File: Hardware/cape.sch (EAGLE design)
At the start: 35 parts, among them IC2 74VHC541, IC4 74VHC541, IC5 74VHC541, J3 RJ45-8P8C, Q1 N-MOSFET-DUALSO8, Q10 N-MOSFET-DUALSO8, Q11 N-MOSFET-DUALSO8, Q12 N-MOSFET-DUALSO8, Q13 N-MOSFET-DUALSO8, Q14 N-MOSFET-DUALSO8, Q15 N-MOSFET-DUALSO8, Q16 N-MOSFET-DUALSO8, Q2 N-MOSFET-DUALSO8, Q3 N-MOSFET-DUALSO8, Q4 N-MOSFET-DUALSO8, Q5 N-MOSFET-DUALSO8, Q6 N-MOSFET-DUALSO8, Q7 N-MOSFET-DUALSO8, Q8 N-MOSFET-DUALSO8, Q9 N-MOSFET-DUALSO8

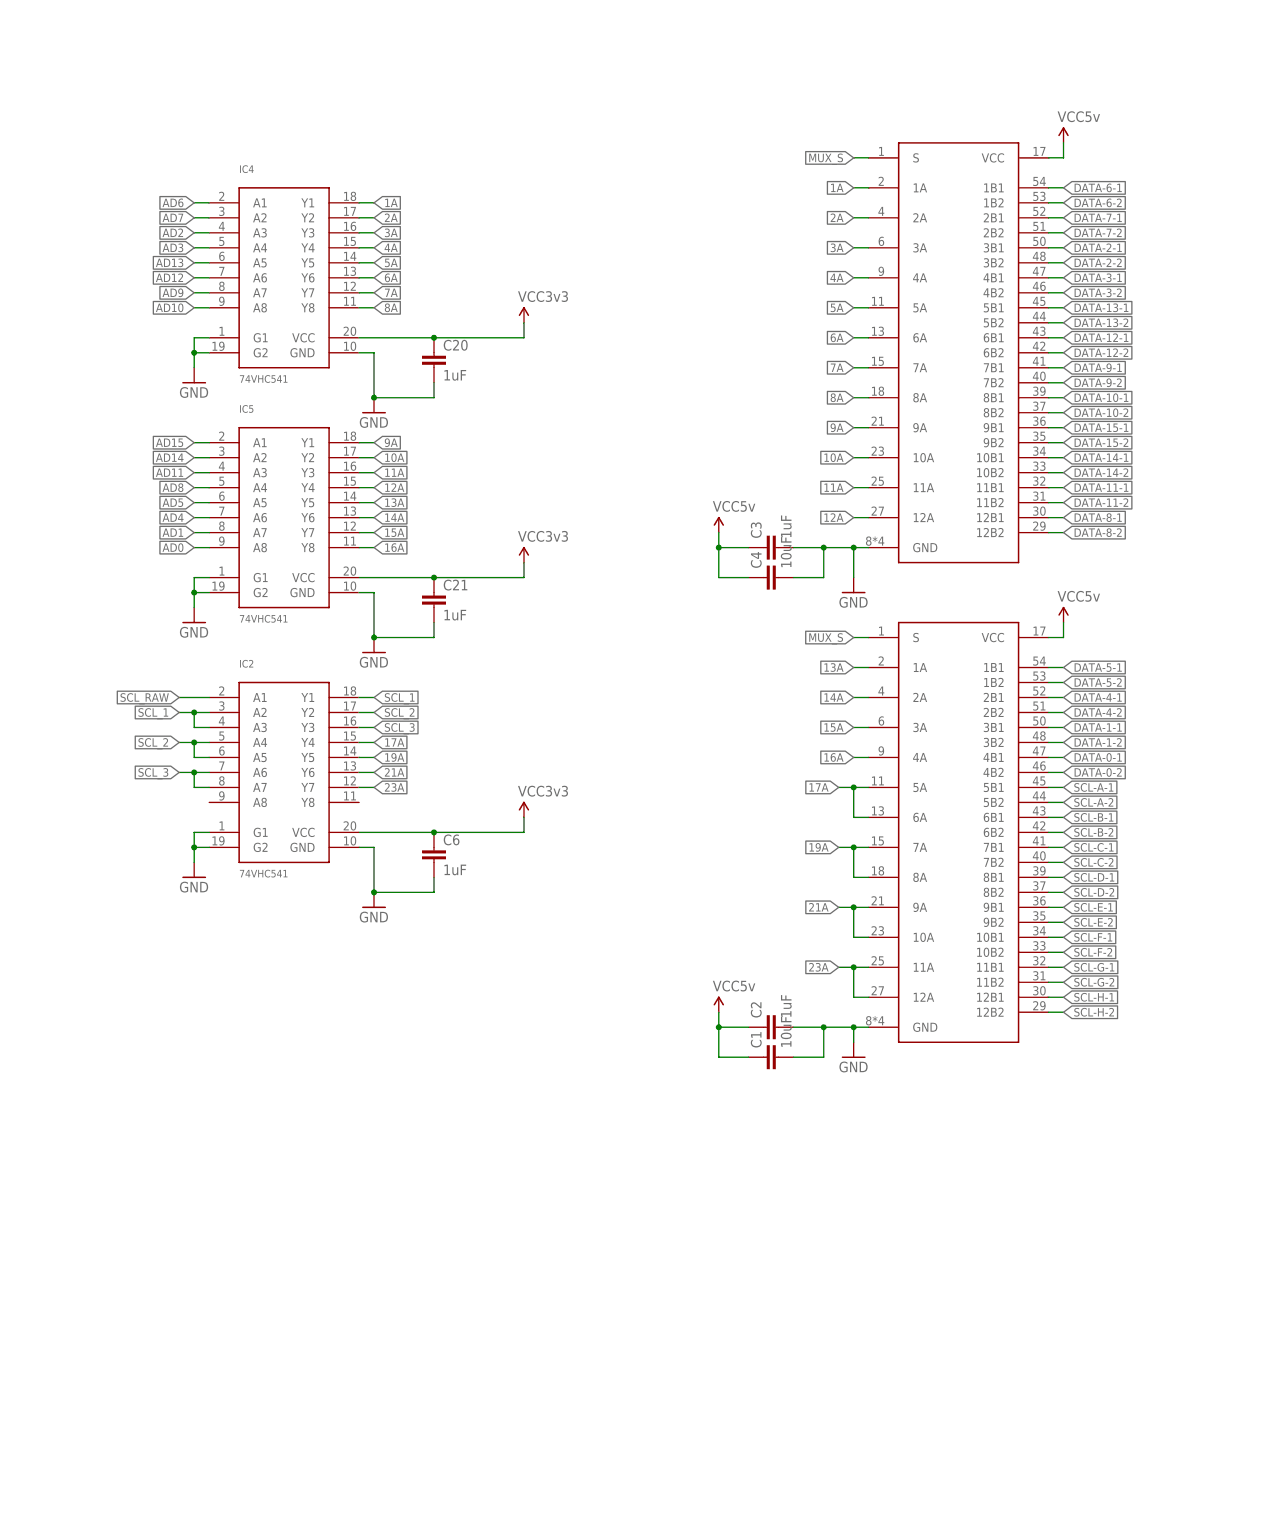
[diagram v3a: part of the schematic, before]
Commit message: Ripped up, starting over with new buffers
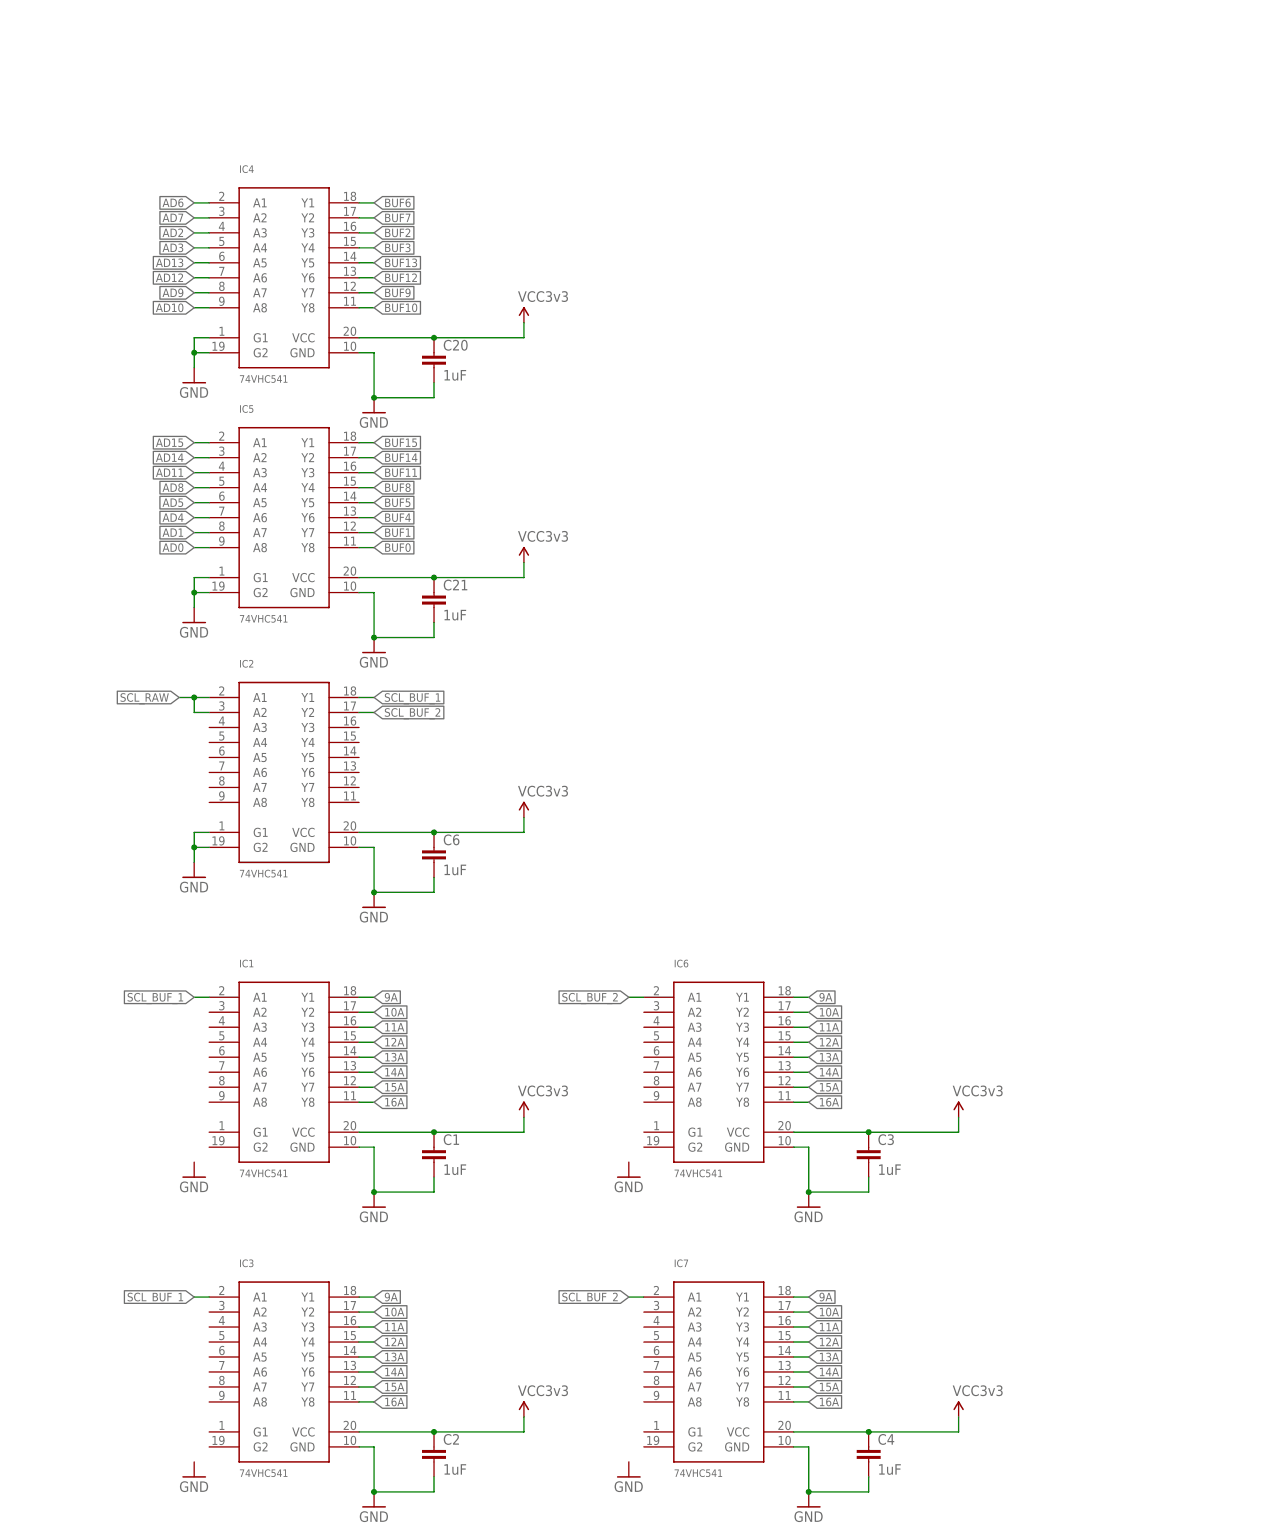
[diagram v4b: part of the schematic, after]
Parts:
- removed U$7, U$8: SN74CBT16292DLRSSOP56, cape:SN74CBT16292DLRSSOP56
- added IC1, IC3, IC6, IC7: 74VHC541, cape:74VHC541
- C1, C4: value 10uF -> 1uF
- IC2, IC4, IC5: PARTNO 74VHC541FT(BE) -> (none)
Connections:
- removed net 17A: IC2.Y4, U$8.5A, U$8.6A
- removed net 19A: IC2.Y5, U$8.7A, U$8.8A
- removed net 1A: IC4.Y1, U$7.1A
- removed net 21A: IC2.Y6, U$8.10A, U$8.9A
- removed net 23A: IC2.Y7, U$8.11A, U$8.12A
- removed net 2A: IC4.Y2, U$7.2A
- removed net 3A: IC4.Y3, U$7.3A
- removed net 4A: IC4.Y4, U$7.4A
- removed net 5A: IC4.Y5, U$7.5A
- removed net 6A: IC4.Y6, U$7.6A
- removed net 7A: IC4.Y7, U$7.7A
- removed net 8A: IC4.Y8, U$7.8A
- removed net SCL_1: IC2.A2, IC2.A3, IC2.Y1
- removed net SCL_2: IC2.A4, IC2.A5, IC2.Y2
- removed net SCL_3: IC2.A6, IC2.A7, IC2.Y3
- new net BUF0: IC5.Y8
- new net BUF1: IC5.Y7
- new net BUF10: IC4.Y8
- new net BUF11: IC5.Y3
- new net BUF12: IC4.Y6
- new net BUF13: IC4.Y5
- new net BUF14: IC5.Y2
- new net BUF15: IC5.Y1
- new net BUF2: IC4.Y3
- new net BUF3: IC4.Y4
- new net BUF4: IC5.Y6
- new net BUF5: IC5.Y5
- new net BUF6: IC4.Y1
- new net BUF7: IC4.Y2
- new net BUF8: IC5.Y4
- new net BUF9: IC4.Y7
- new net SCL_BUF_1: IC1.A1, IC2.Y1, IC3.A1
- new net SCL_BUF_2: IC2.Y2, IC6.A1, IC7.A1
- net 10A: now also IC1.Y2, IC3.Y2, IC6.Y2, IC7.Y2; no longer IC5.Y2, U$7.10A
- net 11A: now also IC1.Y3, IC3.Y3, IC6.Y3, IC7.Y3; no longer IC5.Y3, U$7.11A
- net 12A: now also IC1.Y4, IC3.Y4, IC6.Y4, IC7.Y4; no longer IC5.Y4, U$7.12A
- net 13A: now also IC1.Y5, IC3.Y5, IC6.Y5, IC7.Y5; no longer IC5.Y5, U$8.1A
- net 14A: now also IC1.Y6, IC3.Y6, IC6.Y6, IC7.Y6; no longer IC5.Y6, U$8.2A
- net 15A: now also IC1.Y7, IC3.Y7, IC6.Y7, IC7.Y7; no longer IC5.Y7, U$8.3A
- net 16A: now also IC1.Y8, IC3.Y8, IC6.Y8, IC7.Y8; no longer IC5.Y8, U$8.4A
- net 9A: now also IC1.Y1, IC3.Y1, IC6.Y1, IC7.Y1; no longer IC5.Y1, U$7.9A
- net DATA-0-1: no longer U$8.4B1
- net DATA-0-2: no longer U$8.4B2
- net DATA-1-1: no longer U$8.3B1
- net DATA-1-2: no longer U$8.3B2
- net DATA-10-1: no longer U$7.8B1
- net DATA-10-2: no longer U$7.8B2
- net DATA-11-1: no longer U$7.11B1
- net DATA-11-2: no longer U$7.11B2
- net DATA-12-1: no longer U$7.6B1
- net DATA-12-2: no longer U$7.6B2
- net DATA-13-1: no longer U$7.5B1
- net DATA-13-2: no longer U$7.5B2
- net DATA-14-1: no longer U$7.10B1
- net DATA-14-2: no longer U$7.10B2
- net DATA-15-1: no longer U$7.9B1
- net DATA-15-2: no longer U$7.9B2
- net DATA-2-1: no longer U$7.3B1
- net DATA-2-2: no longer U$7.3B2
- net DATA-3-1: no longer U$7.4B1
- net DATA-3-2: no longer U$7.4B2
- net DATA-4-1: no longer U$8.2B1
- net DATA-4-2: no longer U$8.2B2
- net DATA-5-1: no longer U$8.1B1
- net DATA-5-2: no longer U$8.1B2
- net DATA-6-1: no longer U$7.1B1
- net DATA-6-2: no longer U$7.1B2
- net DATA-7-1: no longer U$7.2B1
- net DATA-7-2: no longer U$7.2B2
- net DATA-8-1: no longer U$7.12B1
- net DATA-8-2: no longer U$7.12B2
- net DATA-9-1: no longer U$7.7B1
- net DATA-9-2: no longer U$7.7B2
- net GND: now also IC1.GND, IC3.GND, IC6.GND, IC7.GND; no longer U$7.GND, U$8.GND
- net MUX_S: no longer U$7.S, U$8.S
- net SCL-A-1: no longer U$8.5B1
- net SCL-A-2: no longer U$8.5B2
- net SCL-B-1: no longer U$8.6B1
- net SCL-B-2: no longer U$8.6B2
- net SCL-C-1: no longer U$8.7B1
- net SCL-C-2: no longer U$8.7B2
- net SCL-D-1: no longer U$8.8B1
- net SCL-D-2: no longer U$8.8B2
- net SCL-E-1: no longer U$8.9B1
- net SCL-E-2: no longer U$8.9B2
- net SCL-F-1: no longer U$8.10B1
- net SCL-F-2: no longer U$8.10B2
- net SCL-G-1: no longer U$8.11B1
- net SCL-G-2: no longer U$8.11B2
- net SCL-H-1: no longer U$8.12B1
- net SCL-H-2: no longer U$8.12B2
- net SCL_RAW: now also IC2.A2
- net VCC3V3: now also C1.1, C2.1, C3.1, C4.1, IC1.VCC, IC3.VCC, IC6.VCC, IC7.VCC
- net VCC5V: no longer C1.1, C2.1, C3.1, C4.1, U$7.VCC, U$8.VCC
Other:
- moved on the sheet: C1, C2, C3, C4

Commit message: Buffer all the things
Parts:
- added C5, C7: 1uF, SparkFun-Capacitors:CAP0805
- added IC8, IC9: 74VHC541, cape:74VHC541
- added R1, R2, R3, R4, R5: RESISTOR-X80603, cape:RESISTOR-X80603
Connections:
- removed net BUF0: IC5.Y8
- removed net BUF1: IC5.Y7
- removed net BUF10: IC4.Y8
- removed net BUF11: IC5.Y3
- removed net BUF12: IC4.Y6
- removed net BUF13: IC4.Y5
- removed net BUF14: IC5.Y2
- removed net BUF15: IC5.Y1
- removed net BUF2: IC4.Y3
- removed net BUF3: IC4.Y4
- removed net BUF4: IC5.Y6
- removed net BUF5: IC5.Y5
- removed net BUF6: IC4.Y1
- removed net BUF7: IC4.Y2
- removed net BUF8: IC5.Y4
- removed net BUF9: IC4.Y7
- removed net DATA-10-1: U$9G$8.1
- removed net DATA-10-2: U$9G$16.1
- removed net DATA-12-1: U$9G$6.1
- removed net DATA-12-2: U$9G$14.1
- removed net DATA-13-1: U$9G$5.1
- removed net DATA-13-2: U$9G$13.1
- removed net DATA-2-1: U$9G$3.1
- removed net DATA-2-2: U$9G$11.1
- removed net DATA-3-1: U$9G$4.1
- removed net DATA-3-2: U$9G$12.1
- removed net DATA-6-1: U$9G$1.1
- removed net DATA-6-2: U$9G$9.1
- removed net DATA-7-1: U$9G$2.1
- removed net DATA-7-2: U$9G$10.1
- removed net DATA-9-1: U$9G$7.1
- removed net DATA-9-2: U$9G$15.1
- removed net SCL_BUF_1: IC1.A1, IC2.Y1, IC3.A1
- removed net SCL_BUF_2: IC2.Y2, IC6.A1, IC7.A1
- new net BUF0_A: R5.7B
- new net BUF0_B: R2.8B, U$9G$8.1
- new net BUF10_A: R4.7B
- new net BUF10_B: R1.8B, U$9G$4.1
- new net BUF11_A: R4.4B
- new net BUF11_B: R2.3B, U$9G$14.1
- new net BUF12_A: R3.2B
- new net BUF12_B: R1.6B, U$9G$3.1
- new net BUF13_A: R3.1B
- new net BUF13_B: R1.5B, U$9G$11.1
- new net BUF14_A: R4.5B
- new net BUF14_B: R2.1B, U$9G$13.1
- new net BUF15_A: R4.6B
- new net BUF15_B: R2.2B, U$9G$5.1
- new net BUF1_A: R5.8B
- new net BUF1_B: R2.7B, U$9G$16.1
- new net BUF2_A: R3.6B
- new net BUF2_B: R1.3B, U$9G$10.1
- new net BUF3_A: R3.5B
- new net BUF3_B: R1.4B, U$9G$2.1
- new net BUF4_A: R4.1B
- new net BUF4_B: R2.6B, U$9G$7.1
- new net BUF5_A: R4.2B
- new net BUF5_B: R2.5B, U$9G$15.1
- new net BUF6_A: R3.8B
- new net BUF6_B: R1.1B, U$9G$9.1
- new net BUF7_A: R3.7B
- new net BUF7_B: R1.2B, U$9G$1.1
- new net BUF8_A: R4.3B
- new net BUF8_B: R2.4B, U$9G$6.1
- new net BUF9_A: R4.8B
- new net BUF9_B: R1.7B, U$9G$12.1
- new net N$1: IC2.A1
- new net N$10: IC8.Y4, R1.4A
- new net N$11: IC8.Y5, R1.5A
- new net N$12: IC8.Y6, R1.6A
- new net N$13: IC8.Y7, R1.7A
- new net N$14: IC8.Y8, R1.8A
- new net N$15: IC9.Y1, R2.1A
- new net N$16: IC9.Y2, R2.2A
- new net N$17: IC9.Y3, R2.3A
- new net N$18: IC9.Y4, R2.4A
- new net N$19: IC9.Y5, R2.5A
- new net N$2: IC2.A2
- new net N$20: IC9.Y6, R2.6A
- new net N$21: IC9.Y7, R2.7A
- new net N$22: IC9.Y8, R2.8A
- new net N$23: IC5.Y1, R4.1A
- new net N$24: IC5.Y2, R4.2A
- new net N$25: IC5.Y3, R4.3A
- new net N$26: IC5.Y4, R4.4A
- new net N$27: IC5.Y6, R4.6A
- new net N$28: IC5.Y5, R4.5A
- new net N$29: IC5.Y7, R4.7A
- new net N$3: IC2.A3
- new net N$30: IC5.Y8, R4.8A
- new net N$31: IC4.Y1, R3.1A
- new net N$32: IC4.Y2, R3.2A
- new net N$34: IC2.Y7, R5.7A
- new net N$35: IC4.Y5, R3.5A
- new net N$36: IC4.Y6, R3.6A
- new net N$37: IC4.Y7, R3.7A
- new net N$38: IC4.Y8, R3.8A
- new net N$39: IC2.Y8, R5.8A
- new net N$4: IC2.A4
- new net N$5: IC2.A5
- new net N$6: IC2.A6
- new net N$7: IC8.Y1, R1.1A
- new net N$8: IC8.Y2, R1.2A
- new net N$9: IC8.Y3, R1.3A
- new net SCL_BUF_A: IC1.A1, IC1.A2, IC1.A3, IC1.A4, IC1.A5, IC1.A6, IC1.A7, IC1.A8, IC3.A1, IC3.A2, IC3.A3, IC3.A4, IC3.A5, IC3.A6, IC3.A7, IC3.A8, IC4.Y3
- new net SCL_BUF_B: IC4.Y4, IC6.A1, IC6.A2, IC6.A3, IC6.A4, IC6.A5, IC6.A6, IC6.A7, IC6.A8, IC7.A1, IC7.A2, IC7.A3, IC7.A4, IC7.A5, IC7.A6, IC7.A7, IC7.A8
- net AD0: now also IC2.A7, IC9.A8; no longer IC5.A8
- net AD1: now also IC2.A8, IC9.A7; no longer IC5.A7
- net AD10: now also IC5.A7, IC8.A8; no longer IC4.A8
- net AD11: now also IC5.A4, IC9.A3; no longer IC5.A3
- net AD12: now also IC4.A2, IC8.A6; no longer IC4.A6
- net AD13: now also IC4.A1, IC8.A5; no longer IC4.A5
- net AD14: now also IC5.A5, IC9.A1; no longer IC5.A2
- net AD15: now also IC5.A6, IC9.A2; no longer IC5.A1
- net AD2: now also IC4.A6, IC8.A3; no longer IC4.A3
- net AD3: now also IC4.A5, IC8.A4; no longer IC4.A4
- net AD4: now also IC5.A1, IC9.A6; no longer IC5.A6
- net AD5: now also IC5.A2, IC9.A5; no longer IC5.A5
- net AD6: now also IC4.A8, IC8.A1; no longer IC4.A1
- net AD7: now also IC4.A7, IC8.A2; no longer IC4.A2
- net AD8: now also IC5.A3, IC9.A4; no longer IC5.A4
- net AD9: now also IC5.A8, IC8.A7; no longer IC4.A7
- net GND: now also C5.2, C7.2, IC8.G1, IC8.G2, IC8.GND, IC9.G1, IC9.G2, IC9.GND
- net SCL_RAW: now also IC4.A3, IC4.A4; no longer IC2.A1, IC2.A2
- net VCC3V3: now also C5.1, C7.1, IC8.VCC, IC9.VCC
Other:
- note added: "BANK A"
- note added: "BANK B"

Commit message: Routing
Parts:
- added R6, R7: RESISTOR-X80603, cape:RESISTOR-X80603
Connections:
- removed net DATA-0-1: U$10G$9.1
- removed net DATA-0-2: U$10G$1.1
- removed net DATA-1-1: U$10G$10.1
- removed net DATA-1-2: U$10G$2.1
- removed net DATA-11-1: U$10G$14.1
- removed net DATA-11-2: U$10G$6.1
- removed net DATA-14-1: U$10G$15.1
- removed net DATA-14-2: U$10G$7.1
- removed net DATA-15-1: U$10G$16.1
- removed net DATA-15-2: U$10G$8.1
- removed net DATA-4-1: U$10G$11.1
- removed net DATA-4-2: U$10G$3.1
- removed net DATA-5-1: U$10G$12.1
- removed net DATA-5-2: U$10G$4.1
- removed net DATA-8-1: U$10G$13.1
- removed net DATA-8-2: U$10G$5.1
- removed net SCL-A-1: U$9G$1.8, U$9G$2.8
- removed net SCL-A-2: U$9G$10.8, U$9G$9.8
- removed net SCL-B-1: U$9G$3.8, U$9G$4.8
- removed net SCL-B-2: U$9G$11.8, U$9G$12.8
- removed net SCL-C-1: U$9G$5.8, U$9G$6.8
- removed net SCL-C-2: U$9G$13.8, U$9G$14.8
- removed net SCL-D-1: U$9G$7.8, U$9G$8.8
- removed net SCL-D-2: U$9G$15.8, U$9G$16.8
- new net N$33: IC6.Y1, R6.1A
- new net N$40: IC6.Y2, R6.2A
- new net N$41: IC6.Y3, R6.3A
- new net N$42: IC6.Y4, R6.4A
- new net N$43: IC6.Y5, R6.5A
- new net N$44: IC6.Y6, R6.6A
- new net N$45: IC6.Y7, R6.7A
- new net N$46: IC6.Y8, R6.8A
- new net N$47: IC7.Y1, R7.1A
- new net N$48: IC7.Y2, R7.2A
- new net N$49: IC7.Y4, R7.4A
- new net N$50: IC7.Y3, R7.3A
- new net N$51: IC7.Y5, R7.5A
- new net N$52: IC7.Y7, R7.7A
- new net N$53: IC7.Y6, R7.6A
- new net N$54: IC7.Y8, R7.8A
- new net SCL0_B: R7.7B, U$9G$16.8
- new net SCL10_B: R6.7B, U$9G$12.8
- new net SCL11_B: R7.4B, U$9G$6.8
- new net SCL12_B: R6.5B, U$9G$11.8
- new net SCL13_B: R6.6B, U$9G$3.8
- new net SCL14_B: R7.2B, U$9G$5.8
- new net SCL15_B: R7.1B, U$9G$13.8
- new net SCL1_B: R7.8B, U$9G$8.8
- new net SCL2_B: R6.4B, U$9G$2.8
- new net SCL3_B: R6.3B, U$9G$10.8
- new net SCL4_B: R7.5B, U$9G$15.8
- new net SCL5_B: R7.6B, U$9G$7.8
- new net SCL6_B: R6.2B, U$9G$1.8
- new net SCL7_B: R6.1B, U$9G$9.8
- new net SCL8_B: R7.3B, U$9G$14.8
- new net SCL9_B: R6.8B, U$9G$4.8
- net 10A: no longer IC6.Y2, IC7.Y2
- net 11A: no longer IC6.Y3, IC7.Y3
- net 12A: no longer IC6.Y4, IC7.Y4
- net 13A: no longer IC6.Y5, IC7.Y5
- net 14A: no longer IC6.Y6, IC7.Y6
- net 15A: no longer IC6.Y7, IC7.Y7
- net 16A: no longer IC6.Y8, IC7.Y8
- net 9A: no longer IC6.Y1, IC7.Y1
- net AD12: now also IC4.A1; no longer IC4.A2
- net AD13: now also IC4.A2; no longer IC4.A1
- net AD14: now also IC5.A6; no longer IC5.A5
- net AD15: now also IC5.A5; no longer IC5.A6
- net BUF0_A: now also U$10G$9.1
- net BUF0_B: now also U$9G$5.1; no longer U$9G$8.1
- net BUF10_A: now also U$10G$13.1
- net BUF10_B: now also U$9G$1.1; no longer U$9G$4.1
- net BUF11_A: now also U$10G$3.1
- net BUF11_B: now also U$9G$15.1; no longer U$9G$14.1
- net BUF12_A: now also R3.1B, U$10G$14.1; no longer R3.2B
- net BUF12_B: now also U$9G$2.1; no longer U$9G$3.1
- net BUF13_A: now also R3.2B, U$10G$6.1; no longer R3.1B
- net BUF13_B: now also U$9G$10.1; no longer U$9G$11.1
- net BUF14_A: now also R4.6B, U$10G$12.1; no longer R4.5B
- net BUF14_B: now also U$9G$16.1; no longer U$9G$13.1
- net BUF15_A: now also R4.5B, U$10G$4.1; no longer R4.6B
- net BUF15_B: now also U$9G$8.1; no longer U$9G$5.1
- net BUF1_A: now also U$10G$1.1
- net BUF1_B: now also U$9G$13.1; no longer U$9G$16.1
- net BUF2_A: now also U$10G$15.1
- net BUF2_B: now also U$9G$11.1; no longer U$9G$10.1
- net BUF3_A: now also U$10G$7.1
- net BUF3_B: now also U$9G$3.1; no longer U$9G$2.1
- net BUF4_A: now also U$10G$10.1
- net BUF4_B: now also U$9G$6.1; no longer U$9G$7.1
- net BUF5_A: now also U$10G$2.1
- net BUF5_B: now also U$9G$14.1; no longer U$9G$15.1
- net BUF6_A: now also U$10G$8.1
- net BUF6_B: now also U$9G$12.1; no longer U$9G$9.1
- net BUF7_A: now also U$10G$16.1
- net BUF7_B: now also U$9G$4.1; no longer U$9G$1.1
- net BUF8_A: now also U$10G$11.1
- net BUF8_B: now also U$9G$7.1; no longer U$9G$6.1
- net BUF9_A: now also U$10G$5.1
- net BUF9_B: now also U$9G$9.1; no longer U$9G$12.1
- net VCC3V3: no longer C1.1, C2.1, C20.1, C21.1, C3.1, C4.1, C5.1, C6.1, C7.1, IC1.VCC, IC2.VCC, IC3.VCC, IC4.VCC, IC5.VCC, IC6.VCC, IC7.VCC, IC8.VCC, IC9.VCC
- net VCC5V: now also C1.1, C2.1, C20.1, C21.1, C3.1, C4.1, C5.1, C6.1, C7.1, IC1.VCC, IC2.VCC, IC3.VCC, IC4.VCC, IC5.VCC, IC6.VCC, IC7.VCC, IC8.VCC, IC9.VCC
